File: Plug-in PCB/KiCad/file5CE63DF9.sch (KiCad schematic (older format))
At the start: 1 part, among them J15 Conn_01x08

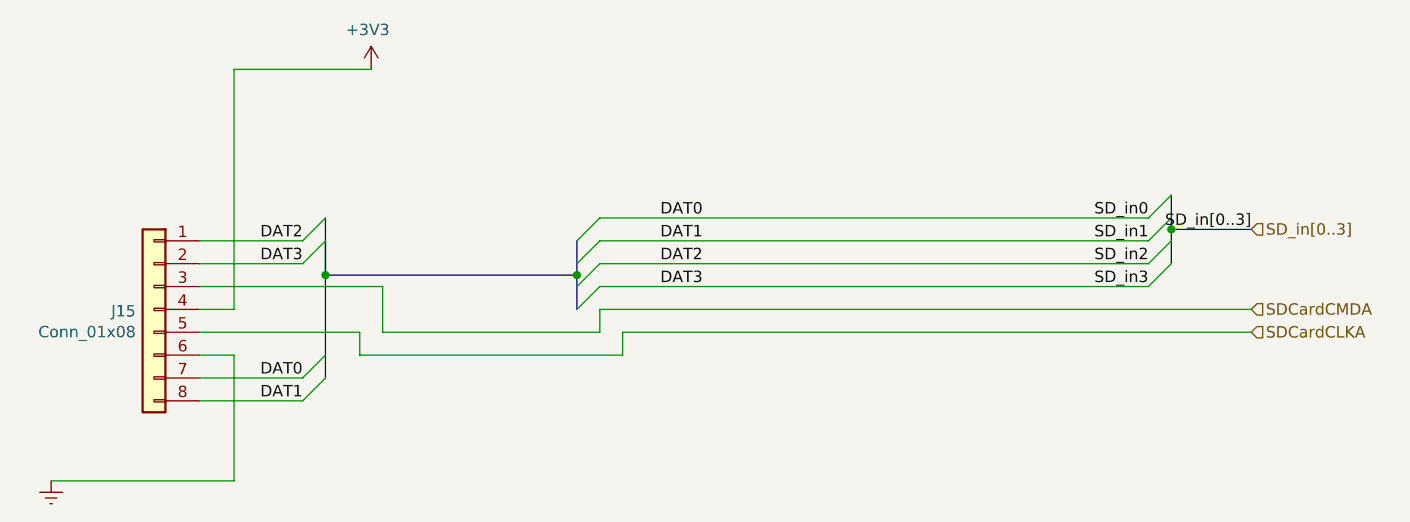
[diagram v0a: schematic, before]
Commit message: Wired Expansion Board Update
1. Begin hardcoding bit-bang communication between wirefree MCU and wired expansion MCU.
++ Can I use the PIO module on the pins to send data in sync while grabbing image from the sensor with parallel capture mode?

2. Wired expansion board schematics and layout modifications
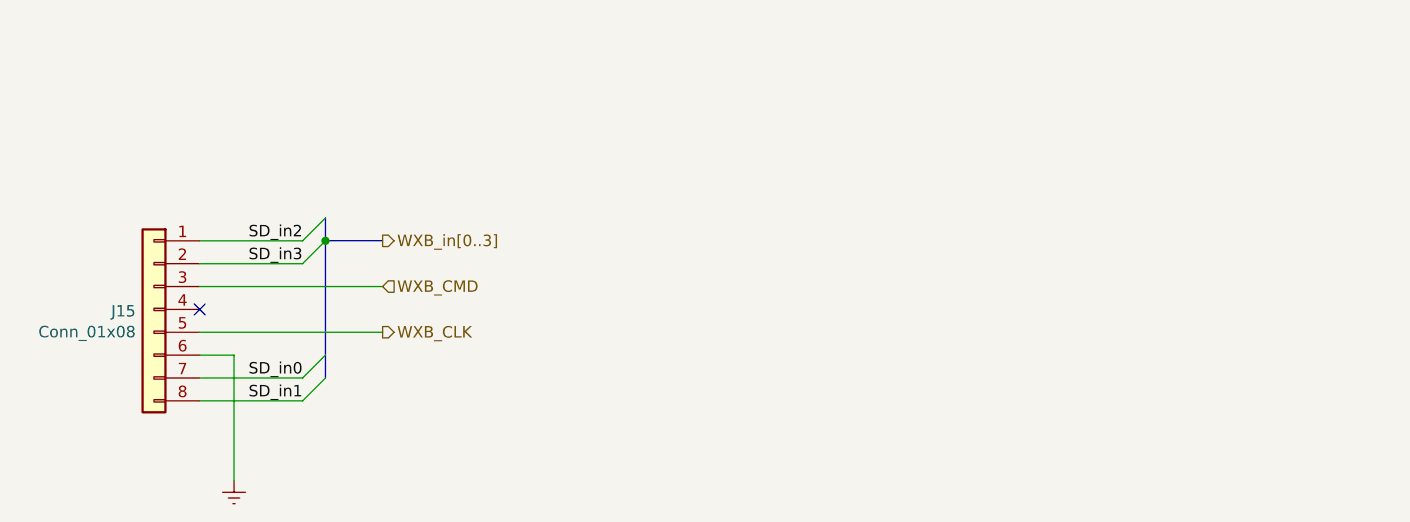
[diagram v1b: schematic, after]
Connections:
- net +3V3: no longer names the net of J15.4 (Pin_4)
- net DAT0 renamed SD_in0
- net DAT1 renamed SD_in1
- net DAT2 renamed SD_in2
- net DAT3 renamed SD_in3
- net SDCardCLKA renamed WXB_CLK
- net SDCardCMDA renamed WXB_CMD
- no-connect marks 0 -> 1
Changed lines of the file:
@@
 $Descr A4 11693 8268
 encoding utf-8
-Sheet 5 6
+Sheet 6 6
 Title ""
 Date ""
@@
 L power:Earth #PWR050
 U 1 1 5C9D8309
-P 2600 4300
-F 0 "#PWR050" H 2600 4050 50  0001 C CNN
-F 1 "Earth" H 2600 4150 50  0001 C CNN
-F 2 "" H 2600 4300 50  0001 C CNN
-F 3 "~" H 2600 4300 50  0001 C CNN
-	1    2600 4300
+P 3400 4300
+F 0 "#PWR050" H 3400 4050 50  0001 C CNN
+F 1 "Earth" H 3400 4150 50  0001 C CNN
+F 2 "" H 3400 4300 50  0001 C CNN
+F 3 "~" H 3400 4300 50  0001 C CNN
+	1    3400 4300
 	-1   0    0    -1
 $EndComp
 Entry Wire Line
 	3800 3250 3700 3350
-$Comp
-L power:+3V3 #PWR048
-U 1 1 5C8E6809
-P 4000 2500
-F 0 "#PWR048" H 4000 2350 50  0001 C CNN
-F 1 "+3V3" H 4015 2673 50  0000 C CNN
-F 2 "" H 4000 2500 50  0001 C CNN
-F 3 "" H 4000 2500 50  0001 C CNN
-	1    4000 2500
-	-1   0    0    -1
-$EndComp
-Text Label 7400 3150 2    50   ~ 0
+Text Label 3700 3850 2    50   ~ 0
 SD_in0
-Entry Wire Line
-	7500 3050 7400 3150
-Entry Wire Line
-	7500 3150 7400 3250
-Entry Wire Line
-	7500 3250 7400 3350
-Entry Wire Line
-	7500 3350 7400 3450
-Wire Bus Line
-	7850 3200 7500 3200
-Text Label 7850 3200 2    50   ~ 0
-SD_in[0..3]
-Wire Bus Line
-	3800 3400 4900 3400
-Connection ~ 3800 3400
-Connection ~ 4900 3400
-Text Label 3700 3850 2    50   ~ 0
-DAT0
 Text Label 3700 3950 2    50   ~ 0
-DAT1
+SD_in1
 Text Label 3700 3250 2    50   ~ 0
-DAT2
+SD_in2
 Text Label 3700 3350 2    50   ~ 0
-DAT3
-Text HLabel 7850 3550 2    50   Input ~ 0
-SDCardCMDA
-Text HLabel 7850 3650 2    50   Input ~ 0
-SDCardCLKA
-Text HLabel 7850 3200 2    50   Input ~ 0
-SD_in[0..3]
-Connection ~ 7500 3200
-Wire Wire Line
-	3400 4300 2600 4300
-Text Label 7400 3250 2    50   ~ 0
-SD_in1
-Text Label 7400 3350 2    50   ~ 0
-SD_in2
-Text Label 7400 3450 2    50   ~ 0
 SD_in3
+Text HLabel 4050 3650 2    50   Output ~ 0
+WXB_CLK
+Text HLabel 4050 3250 2    50   Output ~ 0
+WXB_in[0..3]
 $Comp
 L Connector_Generic:Conn_01x08 J15
@@
 	-1   0    0    -1
 $EndComp
-Wire Wire Line
-	4000 2500 3400 2500
 Wire Wire Line
 	3250 3850 3700 3850
@@
 	3400 3750 3400 4300
 Wire Wire Line
-	4050 3650 4050 3450
+	3250 3650 4050 3650
+Wire Bus Line
+	3800 3150 3800 3250
+Wire Bus Line
+	3800 3250 4050 3250
+Connection ~ 3800 3250
+NoConn ~ 3250 3550
+Wire Bus Line
+	3800 3250 3800 3850
 Wire Wire Line
 	4050 3450 3250 3450
-Wire Wire Line
-	3950 3750 3950 3650
-Wire Wire Line
-	3950 3650 3250 3650
-Wire Wire Line
-	3250 3550 3400 3550
-Wire Wire Line
-	3400 3550 3400 2500
-Wire Wire Line
-	5100 3750 3950 3750
-Wire Wire Line
-	5100 3650 5100 3750
-Wire Wire Line
-	5000 3650 4050 3650
-Wire Wire Line
-	5000 3550 5000 3650
-Entry Wire Line
-	5000 3450 4900 3550
-Entry Wire Line
-	5000 3350 4900 3450
-Entry Wire Line
-	5000 3250 4900 3350
-Entry Wire Line
-	5000 3150 4900 3250
-Text Label 5450 3450 2    50   ~ 0
-DAT3
-Text Label 5450 3350 2    50   ~ 0
-DAT2
-Text Label 5450 3250 2    50   ~ 0
-DAT1
-Text Label 5450 3150 2    50   ~ 0
-DAT0
-Wire Wire Line
-	7850 3550 5000 3550
-Wire Wire Line
-	7400 3450 5000 3450
-Wire Wire Line
-	7400 3350 5000 3350
-Wire Wire Line
-	7400 3250 5000 3250
-Wire Wire Line
-	7400 3150 5000 3150
-Wire Wire Line
-	7850 3650 5100 3650
-Wire Bus Line
-	3800 3250 3800 3400
-Wire Bus Line
-	3800 3150 3800 3400
-Wire Bus Line
-	4900 3400 4900 3550
-Wire Bus Line
-	4900 3250 4900 3400
-Wire Bus Line
-	3800 3400 3800 3850
-Wire Bus Line
-	7500 3200 7500 3350
-Wire Bus Line
-	7500 3050 7500 3200
+Text HLabel 4050 3450 2    50   Input ~ 0
+WXB_CMD
 $EndSCHEMATC

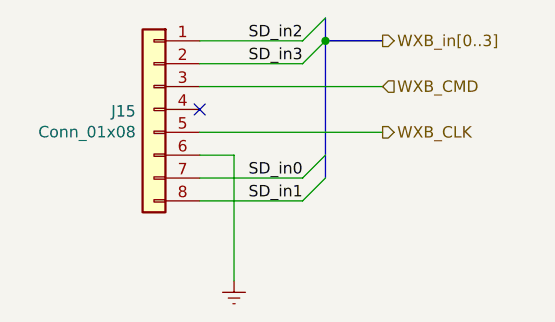
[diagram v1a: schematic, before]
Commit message: Wired Expansion Board Updates
1. KiCad: Schematics and layouts completed/Gerber files generated
2. Atmel: Communication protocol from WireFree to WiredExpansion written
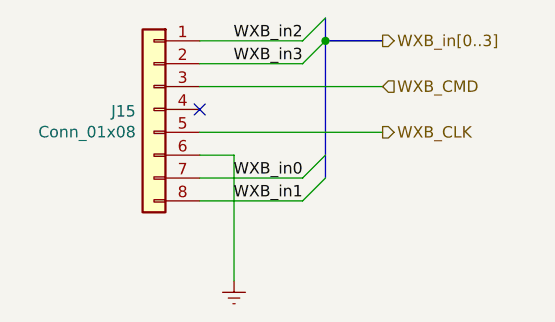
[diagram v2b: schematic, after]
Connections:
- net SD_in0 renamed WXB_in0
- net SD_in1 renamed WXB_in1
- net SD_in2 renamed WXB_in2
- net SD_in3 renamed WXB_in3
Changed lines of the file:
@@
 $Descr A4 11693 8268
 encoding utf-8
-Sheet 6 6
+Sheet 5 6
 Title ""
 Date ""
@@
 	3800 3250 3700 3350
 Text Label 3700 3850 2    50   ~ 0
-SD_in0
+WXB_in0
 Text Label 3700 3950 2    50   ~ 0
-SD_in1
+WXB_in1
 Text Label 3700 3250 2    50   ~ 0
-SD_in2
+WXB_in2
 Text Label 3700 3350 2    50   ~ 0
-SD_in3
+WXB_in3
 Text HLabel 4050 3650 2    50   Output ~ 0
 WXB_CLK
@@
 Connection ~ 3800 3250
 NoConn ~ 3250 3550
-Wire Bus Line
-	3800 3250 3800 3850
 Wire Wire Line
 	4050 3450 3250 3450
 Text HLabel 4050 3450 2    50   Input ~ 0
 WXB_CMD
+Wire Bus Line
+	3800 3250 3800 3850
 $EndSCHEMATC
